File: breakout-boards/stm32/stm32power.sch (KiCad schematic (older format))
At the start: 7 parts

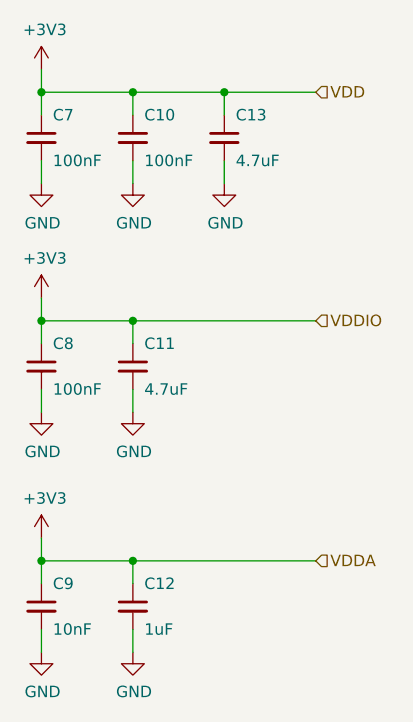
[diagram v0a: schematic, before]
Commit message: (#2) make breakout board for stm32, add 5v sense, reformat pinout, do layout
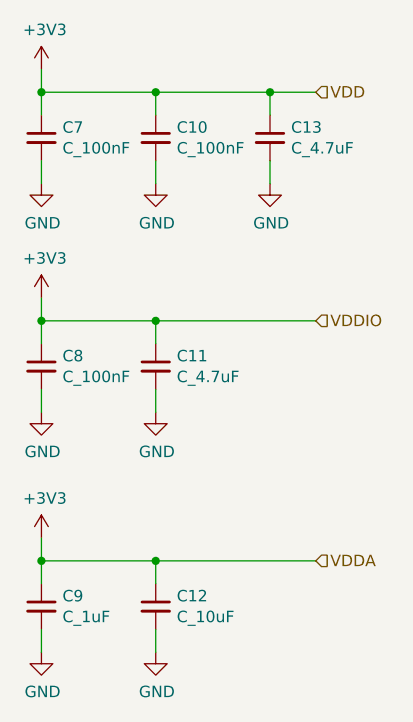
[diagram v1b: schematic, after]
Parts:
- removed C10, C7, C8: 100nF, symbol Device:C_Small
- removed C11, C13: 4.7uF, symbol Device:C_Small
- removed C12: 1uF, symbol Device:C_Small
- removed C9: 10nF, symbol Device:C_Small
- added C10, C7, C8: C_100nF, Capacitor_SMD:C_0201_0603Metric, symbol ultraboard_lib:C_100nF
- added C11, C13: C_4.7uF, Capacitor_SMD:C_0402_1005Metric, symbol ultraboard_lib:C_4.7uF
- added C12: C_10uF, Capacitor_SMD:C_0805_2012Metric, symbol ultraboard_lib:C_10uF
- added C9: C_1uF, Capacitor_SMD:C_0402_1005Metric, symbol ultraboard_lib:C_1uF
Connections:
- net +3V3: now also C10.1, C11.1, C12.1, C13.1, C7.1, C8.1, C9.1
- net GND: now also C10.2, C11.2, C12.2, C13.2, C7.2, C8.2, C9.2
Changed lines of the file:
@@
 VDDIO
 $Comp
-L power:+3V3 #PWR020
+L power:+3V3 #PWR022
 U 1 1 5E0B022E
 P 4600 2400
-F 0 "#PWR020" H 4600 2250 50  0001 C CNN
+F 0 "#PWR022" H 4600 2250 50  0001 C CNN
 F 1 "+3V3" H 4615 2573 50  0000 C CNN
 F 2 "" H 4600 2400 50  0001 C CNN
@@
 $EndComp
 $Comp
-L power:GND #PWR021
+L power:GND #PWR023
 U 1 1 5E0B0DE9
 P 4600 2900
-F 0 "#PWR021" H 4600 2650 50  0001 C CNN
+F 0 "#PWR023" H 4600 2650 50  0001 C CNN
 F 1 "GND" H 4605 2727 50  0000 C CNN
 F 2 "" H 4600 2900 50  0001 C CNN
@@
 	1    0    0    -1
 $EndComp
-$Comp
-L Device:C_Small C7
-U 1 1 5E0B14E2
-P 4600 2700
-F 0 "C7" H 4650 2800 50  0000 L CNN
-F 1 "100nF" H 4650 2600 50  0000 L CNN
-F 2 "" H 4600 2700 50  0001 C CNN
-F 3 "~" H 4600 2700 50  0001 C CNN
-	1    4600 2700
-	1    0    0    -1
-$EndComp
 Wire Wire Line
 	4600 2800 4600 2900
 Wire Wire Line
 	4600 2600 4600 2500
-$Comp
-L Device:C_Small C10
-U 1 1 5E0B19C6
-P 5000 2700
-F 0 "C10" H 5050 2800 50  0000 L CNN
-F 1 "100nF" H 5050 2600 50  0000 L CNN
-F 2 "" H 5000 2700 50  0001 C CNN
-F 3 "~" H 5000 2700 50  0001 C CNN
-	1    5000 2700
-	1    0    0    -1
-$EndComp
-Wire Wire Line
-	5000 2600 5000 2500
-Wire Wire Line
-	5000 2500 4600 2500
+Wire Wire Line
+	5100 2500 4600 2500
 Connection ~ 4600 2500
 Wire Wire Line
 	4600 2500 4600 2400
 $Comp
-L power:GND #PWR026
+L power:GND #PWR028
 U 1 1 5E0B1D99
-P 5000 2900
-F 0 "#PWR026" H 5000 2650 50  0001 C CNN
-F 1 "GND" H 5005 2727 50  0000 C CNN
-F 2 "" H 5000 2900 50  0001 C CNN
-F 3 "" H 5000 2900 50  0001 C CNN
-	1    5000 2900
-	1    0    0    -1
-$EndComp
-Wire Wire Line
-	5000 2900 5000 2800
-$Comp
-L Device:C_Small C13
-U 1 1 5E0B2194
-P 5400 2700
-F 0 "C13" H 5450 2800 50  0000 L CNN
-F 1 "4.7uF" H 5450 2600 50  0000 L CNN
-F 2 "" H 5400 2700 50  0001 C CNN
-F 3 "~" H 5400 2700 50  0001 C CNN
-	1    5400 2700
-	1    0    0    -1
-$EndComp
-$Comp
-L power:GND #PWR029
+P 5100 2900
+F 0 "#PWR028" H 5100 2650 50  0001 C CNN
+F 1 "GND" H 5105 2727 50  0000 C CNN
+F 2 "" H 5100 2900 50  0001 C CNN
+F 3 "" H 5100 2900 50  0001 C CNN
+	1    5100 2900
+	1    0    0    -1
+$EndComp
+Wire Wire Line
+	5100 2900 5100 2800
+$Comp
+L power:GND #PWR031
 U 1 1 5E0B27E4
-P 5400 2900
-F 0 "#PWR029" H 5400 2650 50  0001 C CNN
-F 1 "GND" H 5405 2727 50  0000 C CNN
-F 2 "" H 5400 2900 50  0001 C CNN
-F 3 "" H 5400 2900 50  0001 C CNN
-	1    5400 2900
-	1    0    0    -1
-$EndComp
-Wire Wire Line
-	5400 2900 5400 2800
-Wire Wire Line
-	5400 2600 5400 2500
-Wire Wire Line
-	5400 2500 5000 2500
-Connection ~ 5000 2500
-Wire Wire Line
-	5800 2500 5400 2500
-Connection ~ 5400 2500
-$Comp
-L power:+3V3 #PWR022
+P 5600 2900
+F 0 "#PWR031" H 5600 2650 50  0001 C CNN
+F 1 "GND" H 5605 2727 50  0000 C CNN
+F 2 "" H 5600 2900 50  0001 C CNN
+F 3 "" H 5600 2900 50  0001 C CNN
+	1    5600 2900
+	1    0    0    -1
+$EndComp
+Wire Wire Line
+	5600 2900 5600 2800
+Wire Wire Line
+	5600 2600 5600 2500
+Wire Wire Line
+	5600 2500 5100 2500
+Connection ~ 5100 2500
+Wire Wire Line
+	5800 2500 5600 2500
+Connection ~ 5600 2500
+$Comp
+L power:+3V3 #PWR024
 U 1 1 5E0B5C55
 P 4600 3400
-F 0 "#PWR022" H 4600 3250 50  0001 C CNN
+F 0 "#PWR024" H 4600 3250 50  0001 C CNN
 F 1 "+3V3" H 4615 3573 50  0000 C CNN
 F 2 "" H 4600 3400 50  0001 C CNN
@@
 $EndComp
 $Comp
-L power:GND #PWR023
+L power:GND #PWR025
 U 1 1 5E0B5C5B
 P 4600 3900
-F 0 "#PWR023" H 4600 3650 50  0001 C CNN
+F 0 "#PWR025" H 4600 3650 50  0001 C CNN
 F 1 "GND" H 4605 3727 50  0000 C CNN
 F 2 "" H 4600 3900 50  0001 C CNN
@@
 	1    0    0    -1
 $EndComp
-$Comp
-L Device:C_Small C8
-U 1 1 5E0B5C61
-P 4600 3700
-F 0 "C8" H 4650 3800 50  0000 L CNN
-F 1 "100nF" H 4650 3600 50  0000 L CNN
-F 2 "" H 4600 3700 50  0001 C CNN
-F 3 "~" H 4600 3700 50  0001 C CNN
-	1    4600 3700
-	1    0    0    -1
-$EndComp
 Wire Wire Line
 	4600 3800 4600 3900
 Wire Wire Line
 	4600 3600 4600 3500
-$Comp
-L Device:C_Small C11
-U 1 1 5E0B5C69
-P 5000 3700
-F 0 "C11" H 5050 3800 50  0000 L CNN
-F 1 "4.7uF" H 5050 3600 50  0000 L CNN
-F 2 "" H 5000 3700 50  0001 C CNN
-F 3 "~" H 5000 3700 50  0001 C CNN
-	1    5000 3700
-	1    0    0    -1
-$EndComp
-Wire Wire Line
-	5000 3600 5000 3500
-Wire Wire Line
-	5000 3500 4600 3500
+Wire Wire Line
+	5100 3600 5100 3500
+Wire Wire Line
+	5100 3500 4600 3500
 Connection ~ 4600 3500
 Wire Wire Line
 	4600 3500 4600 3400
 $Comp
-L power:GND #PWR027
+L power:GND #PWR029
 U 1 1 5E0B5C73
-P 5000 3900
-F 0 "#PWR027" H 5000 3650 50  0001 C CNN
-F 1 "GND" H 5005 3727 50  0000 C CNN
-F 2 "" H 5000 3900 50  0001 C CNN
-F 3 "" H 5000 3900 50  0001 C CNN
-	1    5000 3900
-	1    0    0    -1
-$EndComp
-Wire Wire Line
-	5000 3900 5000 3800
-Connection ~ 5000 3500
-Wire Wire Line
-	5000 3500 5800 3500
-$Comp
-L power:+3V3 #PWR024
+P 5100 3900
+F 0 "#PWR029" H 5100 3650 50  0001 C CNN
+F 1 "GND" H 5105 3727 50  0000 C CNN
+F 2 "" H 5100 3900 50  0001 C CNN
+F 3 "" H 5100 3900 50  0001 C CNN
+	1    5100 3900
+	1    0    0    -1
+$EndComp
+Wire Wire Line
+	5100 3900 5100 3800
+Connection ~ 5100 3500
+Wire Wire Line
+	5100 3500 5800 3500
+$Comp
+L power:+3V3 #PWR026
 U 1 1 5E0B793D
 P 4600 4450
-F 0 "#PWR024" H 4600 4300 50  0001 C CNN
+F 0 "#PWR026" H 4600 4300 50  0001 C CNN
 F 1 "+3V3" H 4615 4623 50  0000 C CNN
 F 2 "" H 4600 4450 50  0001 C CNN
@@
 $EndComp
 $Comp
-L power:GND #PWR025
+L power:GND #PWR027
 U 1 1 5E0B7943
 P 4600 4950
-F 0 "#PWR025" H 4600 4700 50  0001 C CNN
+F 0 "#PWR027" H 4600 4700 50  0001 C CNN
 F 1 "GND" H 4605 4777 50  0000 C CNN
 F 2 "" H 4600 4950 50  0001 C CNN
@@
 	1    0    0    -1
 $EndComp
-$Comp
-L Device:C_Small C9
-U 1 1 5E0B7949
+Wire Wire Line
+	4600 4850 4600 4950
+Wire Wire Line
+	4600 4650 4600 4550
+Wire Wire Line
+	5100 4650 5100 4550
+Wire Wire Line
+	5100 4550 4600 4550
+Connection ~ 4600 4550
+Wire Wire Line
+	4600 4550 4600 4450
+$Comp
+L power:GND #PWR030
+U 1 1 5E0B795B
+P 5100 4950
+F 0 "#PWR030" H 5100 4700 50  0001 C CNN
+F 1 "GND" H 5105 4777 50  0000 C CNN
+F 2 "" H 5100 4950 50  0001 C CNN
+F 3 "" H 5100 4950 50  0001 C CNN
+	1    5100 4950
+	1    0    0    -1
+$EndComp
+Wire Wire Line
+	5100 4950 5100 4850
+Connection ~ 5100 4550
+Wire Wire Line
+	5100 4550 5800 4550
+$Comp
+L ultraboard_lib:C_100nF C7
+U 1 1 5E12DEC9
+P 4600 2700
+F 0 "C7" H 4692 2746 50  0000 L CNN
+F 1 "C_100nF" H 4692 2655 50  0000 L CNN
+F 2 "Capacitor_SMD:C_0201_0603Metric" H 4775 2700 50  0001 C CNN
+F 3 "" H 4775 2700 50  0001 C CNN
+	1    4600 2700
+	1    0    0    -1
+$EndComp
+$Comp
+L ultraboard_lib:C_100nF C10
+U 1 1 5E12E64C
+P 5100 2700
+F 0 "C10" H 5192 2746 50  0000 L CNN
+F 1 "C_100nF" H 5192 2655 50  0000 L CNN
+F 2 "Capacitor_SMD:C_0201_0603Metric" H 5275 2700 50  0001 C CNN
+F 3 "" H 5275 2700 50  0001 C CNN
+	1    5100 2700
+	1    0    0    -1
+$EndComp
+Wire Wire Line
+	5100 2600 5100 2500
+$Comp
+L ultraboard_lib:C_100nF C8
+U 1 1 5E12ED46
+P 4600 3700
+F 0 "C8" H 4692 3746 50  0000 L CNN
+F 1 "C_100nF" H 4692 3655 50  0000 L CNN
+F 2 "Capacitor_SMD:C_0201_0603Metric" H 4775 3700 50  0001 C CNN
+F 3 "" H 4775 3700 50  0001 C CNN
+	1    4600 3700
+	1    0    0    -1
+$EndComp
+$Comp
+L ultraboard_lib:C_4.7uF C11
+U 1 1 5E13277C
+P 5100 3700
+F 0 "C11" H 5192 3746 50  0000 L CNN
+F 1 "C_4.7uF" H 5192 3655 50  0000 L CNN
+F 2 "Capacitor_SMD:C_0402_1005Metric" H 5375 3750 50  0001 C CNN
+F 3 "" H 5250 3700 50  0001 C CNN
+	1    5100 3700
+	1    0    0    -1
+$EndComp
+$Comp
+L ultraboard_lib:C_4.7uF C13
+U 1 1 5E1327F1
+P 5600 2700
+F 0 "C13" H 5692 2746 50  0000 L CNN
+F 1 "C_4.7uF" H 5692 2655 50  0000 L CNN
+F 2 "Capacitor_SMD:C_0402_1005Metric" H 5875 2750 50  0001 C CNN
+F 3 "" H 5750 2700 50  0001 C CNN
+	1    5600 2700
+	1    0    0    -1
+$EndComp
+$Comp
+L ultraboard_lib:C_1uF C9
+U 1 1 5E13326B
 P 4600 4750
-F 0 "C9" H 4650 4850 50  0000 L CNN
-F 1 "10nF" H 4650 4650 50  0000 L CNN
-F 2 "" H 4600 4750 50  0001 C CNN
-F 3 "~" H 4600 4750 50  0001 C CNN
+F 0 "C9" H 4692 4796 50  0000 L CNN
+F 1 "C_1uF" H 4692 4705 50  0000 L CNN
+F 2 "Capacitor_SMD:C_0402_1005Metric" H 4875 4800 50  0001 C CNN
+F 3 "" H 4750 4750 50  0001 C CNN
 	1    4600 4750
 	1    0    0    -1
 $EndComp
-Wire Wire Line
-	4600 4850 4600 4950
-Wire Wire Line
-	4600 4650 4600 4550
-$Comp
-L Device:C_Small C12
-U 1 1 5E0B7951
-P 5000 4750
-F 0 "C12" H 5050 4850 50  0000 L CNN
-F 1 "1uF" H 5050 4650 50  0000 L CNN
-F 2 "" H 5000 4750 50  0001 C CNN
-F 3 "~" H 5000 4750 50  0001 C CNN
-	1    5000 4750
-	1    0    0    -1
-$EndComp
-Wire Wire Line
-	5000 4650 5000 4550
-Wire Wire Line
-	5000 4550 4600 4550
-Connection ~ 4600 4550
-Wire Wire Line
-	4600 4550 4600 4450
-$Comp
-L power:GND #PWR028
-U 1 1 5E0B795B
-P 5000 4950
-F 0 "#PWR028" H 5000 4700 50  0001 C CNN
-F 1 "GND" H 5005 4777 50  0000 C CNN
-F 2 "" H 5000 4950 50  0001 C CNN
-F 3 "" H 5000 4950 50  0001 C CNN
-	1    5000 4950
-	1    0    0    -1
-$EndComp
-Wire Wire Line
-	5000 4950 5000 4850
-Connection ~ 5000 4550
-Wire Wire Line
-	5000 4550 5800 4550
+$Comp
+L ultraboard_lib:C_10uF C12
+U 1 1 5E133989
+P 5100 4750
+F 0 "C12" H 5192 4796 50  0000 L CNN
+F 1 "C_10uF" H 5192 4705 50  0000 L CNN
+F 2 "Capacitor_SMD:C_0805_2012Metric" H 5100 4750 50  0001 C CNN
+F 3 "" H 5100 4750 50  0001 C CNN
+	1    5100 4750
+	1    0    0    -1
+$EndComp
 $EndSCHEMATC

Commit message: (#14) redo stm32 and eeprom board to only include 0603 and 0805 components
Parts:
- C10, C7, C8: footprint Capacitor_SMD:C_0201_0603Metric -> Capacitor_SMD:C_0603_1608Metric
- C11, C13, C9: footprint Capacitor_SMD:C_0402_1005Metric -> Capacitor_SMD:C_0603_1608Metric
- C12: footprint Capacitor_SMD:C_0805_2012Metric -> Capacitor_SMD:C_0603_1608Metric
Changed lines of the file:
@@
 Sheet 2 2
 Title "STM32F042K6 Power Pins"
-Date "2019-12-30"
-Rev "A"
+Date "2020-02-07"
+Rev "B"
 Comp "The Ultraboard Project"
 Comment1 "https://www.gnu.org/licenses/gpl-3.0.en.html"
@@
 F 0 "C7" H 4692 2746 50  0000 L CNN
 F 1 "C_100nF" H 4692 2655 50  0000 L CNN
-F 2 "Capacitor_SMD:C_0201_0603Metric" H 4775 2700 50  0001 C CNN
+F 2 "Capacitor_SMD:C_0603_1608Metric" H 4775 2700 50  0001 C CNN
 F 3 "" H 4775 2700 50  0001 C CNN
 	1    4600 2700
@@
 F 0 "C10" H 5192 2746 50  0000 L CNN
 F 1 "C_100nF" H 5192 2655 50  0000 L CNN
-F 2 "Capacitor_SMD:C_0201_0603Metric" H 5275 2700 50  0001 C CNN
+F 2 "Capacitor_SMD:C_0603_1608Metric" H 5275 2700 50  0001 C CNN
 F 3 "" H 5275 2700 50  0001 C CNN
 	1    5100 2700
@@
 F 0 "C8" H 4692 3746 50  0000 L CNN
 F 1 "C_100nF" H 4692 3655 50  0000 L CNN
-F 2 "Capacitor_SMD:C_0201_0603Metric" H 4775 3700 50  0001 C CNN
+F 2 "Capacitor_SMD:C_0603_1608Metric" H 4775 3700 50  0001 C CNN
 F 3 "" H 4775 3700 50  0001 C CNN
 	1    4600 3700
@@
 F 0 "C11" H 5192 3746 50  0000 L CNN
 F 1 "C_4.7uF" H 5192 3655 50  0000 L CNN
-F 2 "Capacitor_SMD:C_0402_1005Metric" H 5375 3750 50  0001 C CNN
+F 2 "Capacitor_SMD:C_0603_1608Metric" H 5375 3750 50  0001 C CNN
 F 3 "" H 5250 3700 50  0001 C CNN
 	1    5100 3700
@@
 F 0 "C13" H 5692 2746 50  0000 L CNN
 F 1 "C_4.7uF" H 5692 2655 50  0000 L CNN
-F 2 "Capacitor_SMD:C_0402_1005Metric" H 5875 2750 50  0001 C CNN
+F 2 "Capacitor_SMD:C_0603_1608Metric" H 5875 2750 50  0001 C CNN
 F 3 "" H 5750 2700 50  0001 C CNN
 	1    5600 2700
@@
 F 0 "C9" H 4692 4796 50  0000 L CNN
 F 1 "C_1uF" H 4692 4705 50  0000 L CNN
-F 2 "Capacitor_SMD:C_0402_1005Metric" H 4875 4800 50  0001 C CNN
+F 2 "Capacitor_SMD:C_0603_1608Metric" H 4875 4800 50  0001 C CNN
 F 3 "" H 4750 4750 50  0001 C CNN
 	1    4600 4750
@@
 F 0 "C12" H 5192 4796 50  0000 L CNN
 F 1 "C_10uF" H 5192 4705 50  0000 L CNN
-F 2 "Capacitor_SMD:C_0805_2012Metric" H 5100 4750 50  0001 C CNN
+F 2 "Capacitor_SMD:C_0603_1608Metric" H 5100 4750 50  0001 C CNN
 F 3 "" H 5100 4750 50  0001 C CNN
 	1    5100 4750
